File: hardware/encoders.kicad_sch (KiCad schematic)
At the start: 10 parts, among them SW1 EC11, SW2 EC11, SW3 EC11, SW4 EC11, SW5 EC11, SW6 EC11, SW7 EC11, SW8 EC11, U4 MCP23017

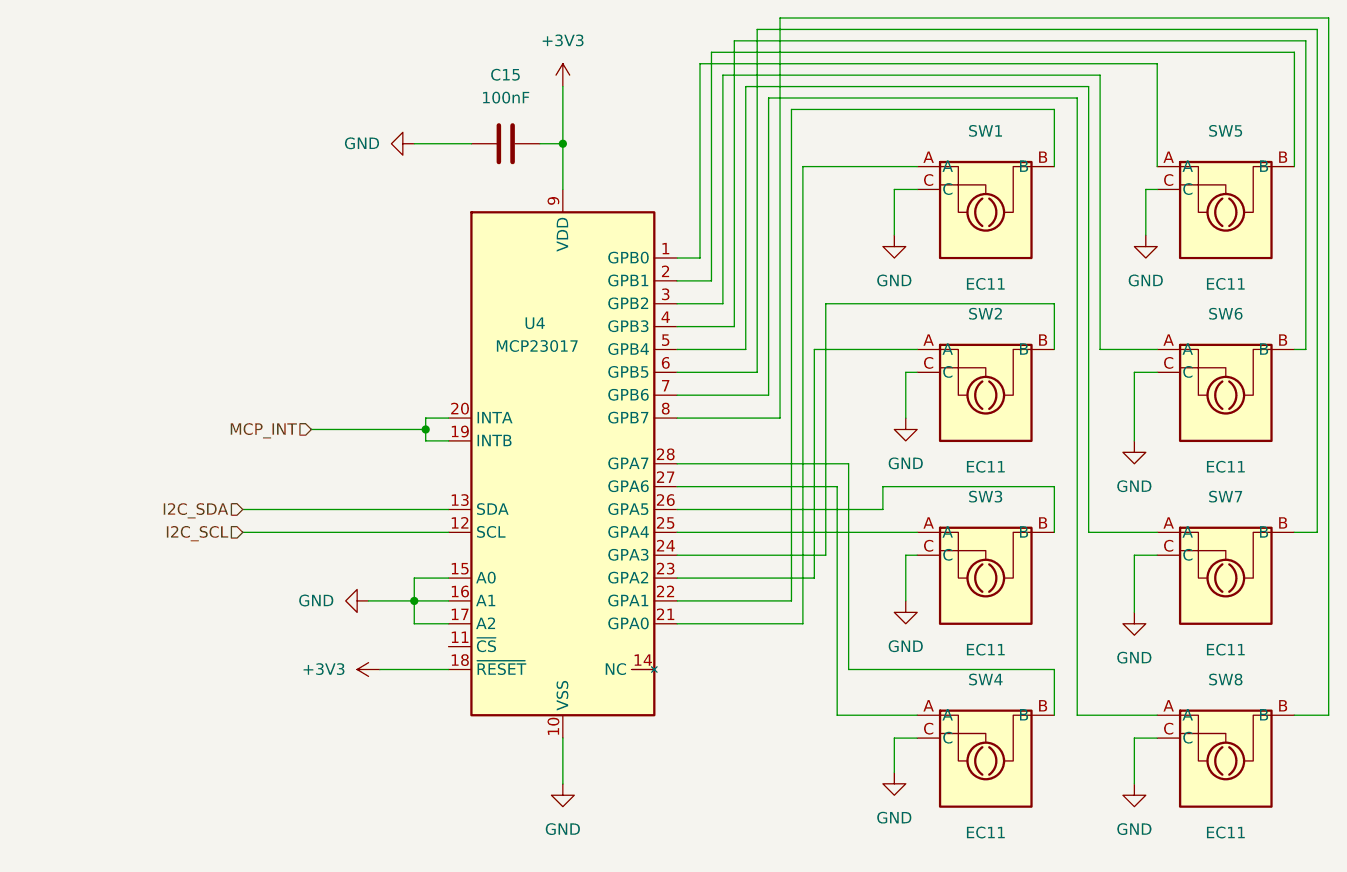
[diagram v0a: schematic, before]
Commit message: Complete hierarchical schematic sheets and fix wiring
- Complete encoder_leds sheet with MAX7219 + 64 LEDs
- Complete ui_leds sheet with MAX7219 + 45 LEDs
- Complete buttons sheet with MCP23017 + 40 buttons
- Complete display sheet with OLED I2C connector
- Complete pots sheet with 3 potentiometers
- Complete encoders sheet with 8 rotary encoders on MCP23017
- Fix inputs sheet hierarchical labels (CLK_IN, RST_IN, SCENE_CV_IN)
- Update MCU sheet with ADC hierarchical labels
- Update root sheet with hierarchical pin connections
- Various ERC fixes and wiring corrections

Co-Authored-By: Claude Opus 4.5 <noreply@anthropic.com>
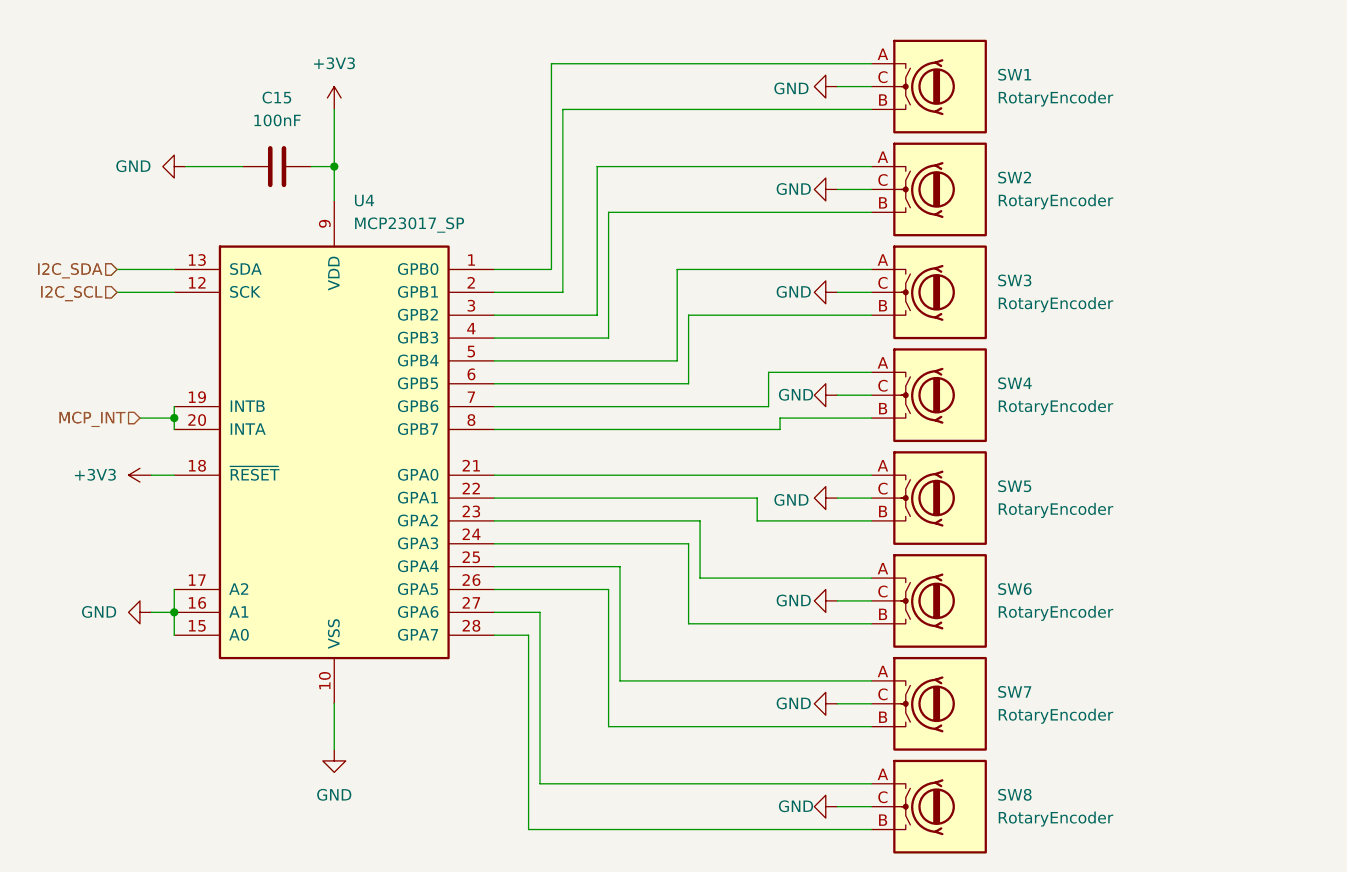
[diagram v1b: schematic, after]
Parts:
- removed SW1, SW2, SW3, SW4, SW5, SW6, SW7, SW8: EC11, Rotary_Encoder:RotaryEncoder_Alps_EC11E-Switch_Vertical_H20mm, symbol Device:Rotary_Encoder
- added SW1, SW2, SW3, SW4, SW5, SW6, SW7, SW8: RotaryEncoder, Rotary_Encoder:RotaryEncoder_Alps_EC12E_Vertical_H20mm_CircularMountingHoles, symbol Device:RotaryEncoder
- U4: value MCP23017 -> MCP23017_SP
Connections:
- net GND: now also SW1.C, SW2.C, SW3.C, SW4.C, SW5.C, SW6.C, SW7.C, SW8.C
- net at U4.3 (GPB2): now also SW2.A
- net at U4.4 (GPB3): now also SW2.B
- net at U4.1 (GPB0): now also SW1.A
- net at U4.2 (GPB1): now also SW1.B
- net at U4.21 (GPA0): now also SW5.A
- net at U4.22 (GPA1): now also SW5.B
- net at U4.23 (GPA2): now also SW6.A
- net at U4.24 (GPA3): now also SW6.B
- net at U4.25 (GPA4): now also SW7.A
- net at U4.26 (GPA5): now also SW7.B
- net at U4.27 (GPA6): now also SW8.A
- net at U4.28 (GPA7): now also SW8.B
- net at U4.5 (GPB4): now also SW3.A
- net at U4.6 (GPB5): now also SW3.B
- net at U4.7 (GPB6): now also SW4.A
- net at U4.8 (GPB7): now also SW4.B
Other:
- moved on the sheet: C15

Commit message: Assign footprints to all schematic components
SMD footprints assigned:
- Capacitors: 0402 (20pF), 0603 (100nF), 0805 (10uF), 1206 (47uF, 100uF)
- Resistors: 0603
- LEDs: 0201
- MAX7219: SOIC-24W
- ULN2003: SOIC-16
- Switches: TL3342 tactile
- Connectors: JST PH, pin headers

Also removes accidentally committed autosave files.

Co-Authored-By: Claude Opus 4.5 <noreply@anthropic.com>
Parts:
- C15: footprint (none) -> Capacitor_SMD:C_0603_1608Metric
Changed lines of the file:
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@@
 			)
 		)
-		(property "Footprint" ""
+		(property "Footprint" "Capacitor_SMD:C_0603_1608Metric"
 			(at 96.52 70.1548 0)
 			(effects
